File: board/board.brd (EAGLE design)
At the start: 94 x 44.5 mm, 71 parts, among them Q2 ULN2003AD

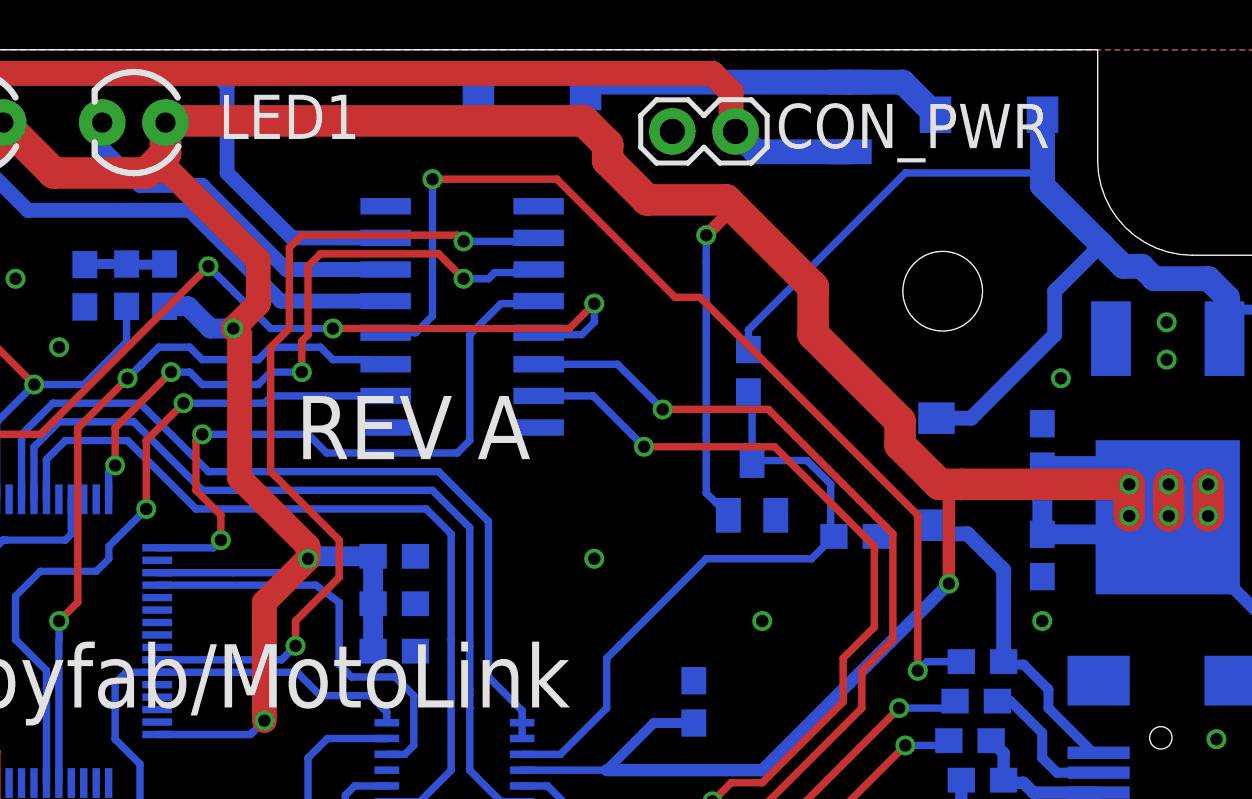
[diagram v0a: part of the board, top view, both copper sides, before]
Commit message: [Board] Adding output for external relay
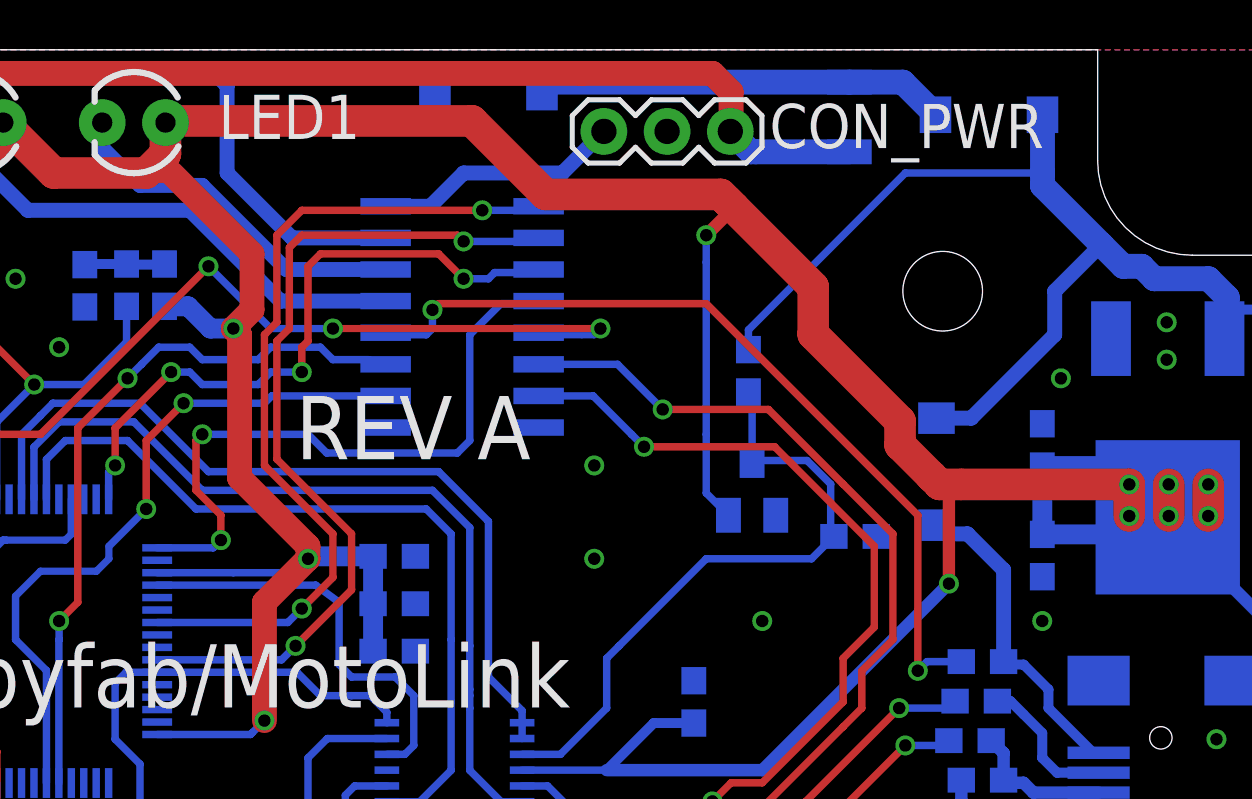
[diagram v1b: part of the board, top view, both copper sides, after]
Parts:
- CON_PWR: value M02PTH -> (none); device SparkFun-Connectors:1X02 -> SparkFun-Connectors:1X03
- IC_REG: value LD117ADT33TR -> NCV4274DT33RKG
- Y1: value (none) -> 8Mhz
- moved CON_PWR 2.75 mm to (65.9, 41.2)
- moved TVS1 1.75 mm to (61.2, 42.8)
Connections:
- new net RELAY_OUT: CON_PWR.1, Q2.16
- new net RELAY_TRIG: Q2.1, STM32.23
- net +12V: now also CON_PWR.3; no longer CON_PWR.2
- net GND: now also CON_PWR.2; no longer CON_PWR.1
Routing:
- net RELAY_TRIG: track 0.00 -> 33.9 mm, vias 0 -> 2
- net RELAY_OUT: track 0.00 -> 10.0 mm
- net N$7: track 40.9 -> 34.0 mm
- net N$9: track 14.8 -> 16.5 mm
- net USB_VBUS_CTRL: track 37.1 -> 36.3 mm

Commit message: [Board] Updated parts references
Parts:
- D1, D5, D6: value (none) -> B240A
- IC_REG: value NCV4274DT33RKG -> LM1117-3.3
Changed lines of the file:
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@@
 </autorouter>
 <elements>
-<element name="IC_REG" library="v-reg" package="DPACK" value="NCV4274DT33RKG" x="88.5425" y="28.045" smashed="yes" rot="MR180">
+<element name="IC_REG" library="v-reg" package="DPACK" value="LM1117-3.3" x="88.5425" y="28.045" smashed="yes" rot="MR180">
 <attribute name="NAME" x="84.3" y="22.33" size="1.778" layer="26" font="vector" ratio="16" rot="MR180"/>
 <attribute name="VALUE" x="93.6225" y="30.585" size="1.27" layer="28" rot="MR270"/>
@@
 <attribute name="VALUE" x="84.6455" y="25.146" size="0.4064" layer="28" font="vector" rot="MR270"/>
 </element>
-<element name="D1" library="SparkFun-DiscreteSemi" package="SMA-DIODE" value="" x="81.36" y="41.84" smashed="yes" rot="MR180">
+<element name="D1" library="SparkFun-DiscreteSemi" package="SMA-DIODE" value="B240A" x="81.36" y="41.84" smashed="yes" rot="MR180">
 <attribute name="NAME" x="81.824" y="39.939" size="1.778" layer="26" font="vector" ratio="16" rot="MR180"/>
 <attribute name="VALUE" x="81.614" y="40.189" size="0.4064" layer="28" rot="MR180"/>
@@
 <attribute name="VALUE" x="35.984" y="5.393" size="0.4064" layer="28" font="vector" rot="MR180"/>
 </element>
-<element name="D5" library="SparkFun-DiscreteSemi" package="SMA-DIODE" value="" x="79.25" y="27.5" smashed="yes" rot="MR90">
+<element name="D5" library="SparkFun-DiscreteSemi" package="SMA-DIODE" value="B240A" x="79.25" y="27.5" smashed="yes" rot="MR90">
 <attribute name="NAME" x="75.651" y="26.464" size="1.778" layer="26" font="vector" ratio="16" rot="MR90"/>
 <attribute name="VALUE" x="80.901" y="27.754" size="0.4064" layer="28" rot="MR90"/>
@@
 <attribute name="VALUE" x="10.516" y="23.107" size="0.4064" layer="28" font="vector" rot="MR0"/>
 </element>
-<element name="D6" library="SparkFun-DiscreteSemi" package="SMA-DIODE" value="" x="2.25" y="20.5" smashed="yes" rot="MR90">
+<element name="D6" library="SparkFun-DiscreteSemi" package="SMA-DIODE" value="B240A" x="2.25" y="20.5" smashed="yes" rot="MR90">
 <attribute name="NAME" x="3.901" y="18.964" size="1.778" layer="26" font="vector" ratio="16" rot="MR90"/>
 <attribute name="VALUE" x="3.901" y="20.754" size="0.4064" layer="28" rot="MR90"/>

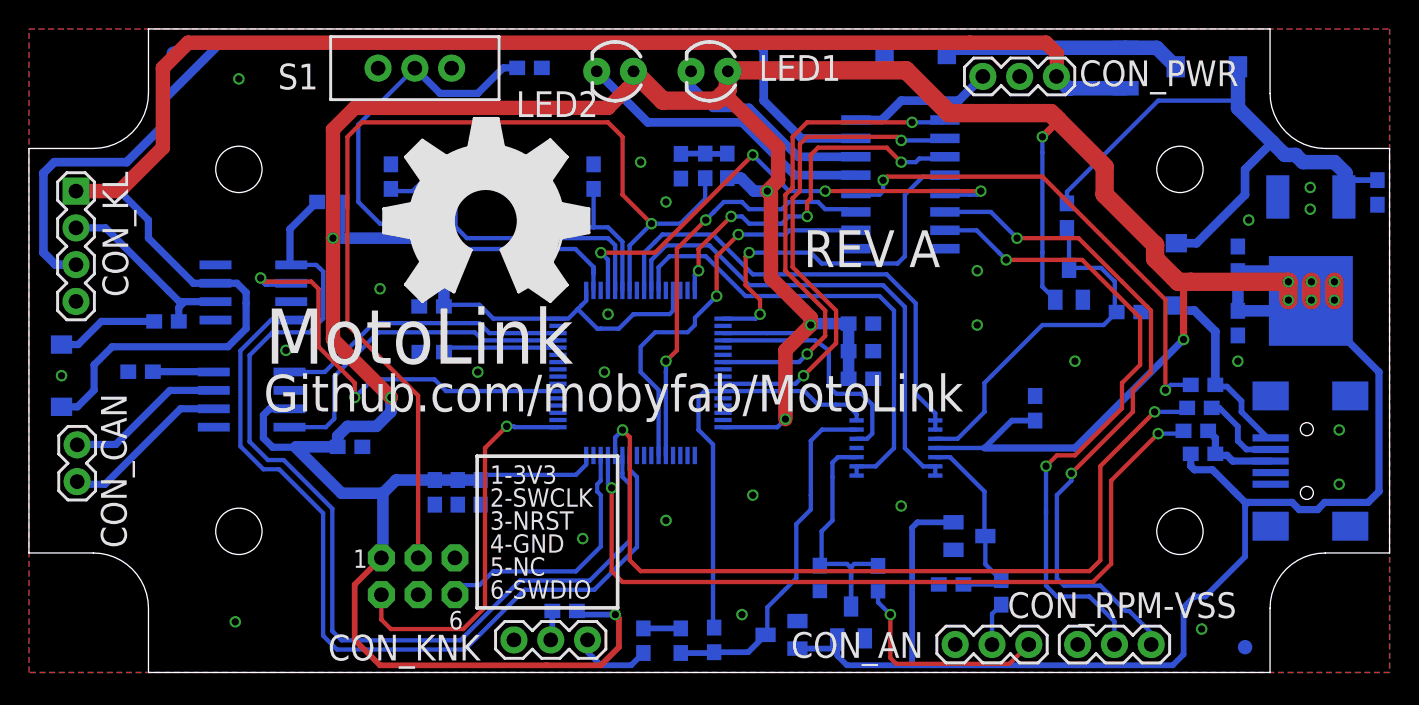
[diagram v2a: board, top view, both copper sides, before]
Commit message: [Board] Updated USB with esd/tvs protection, and vbus detection
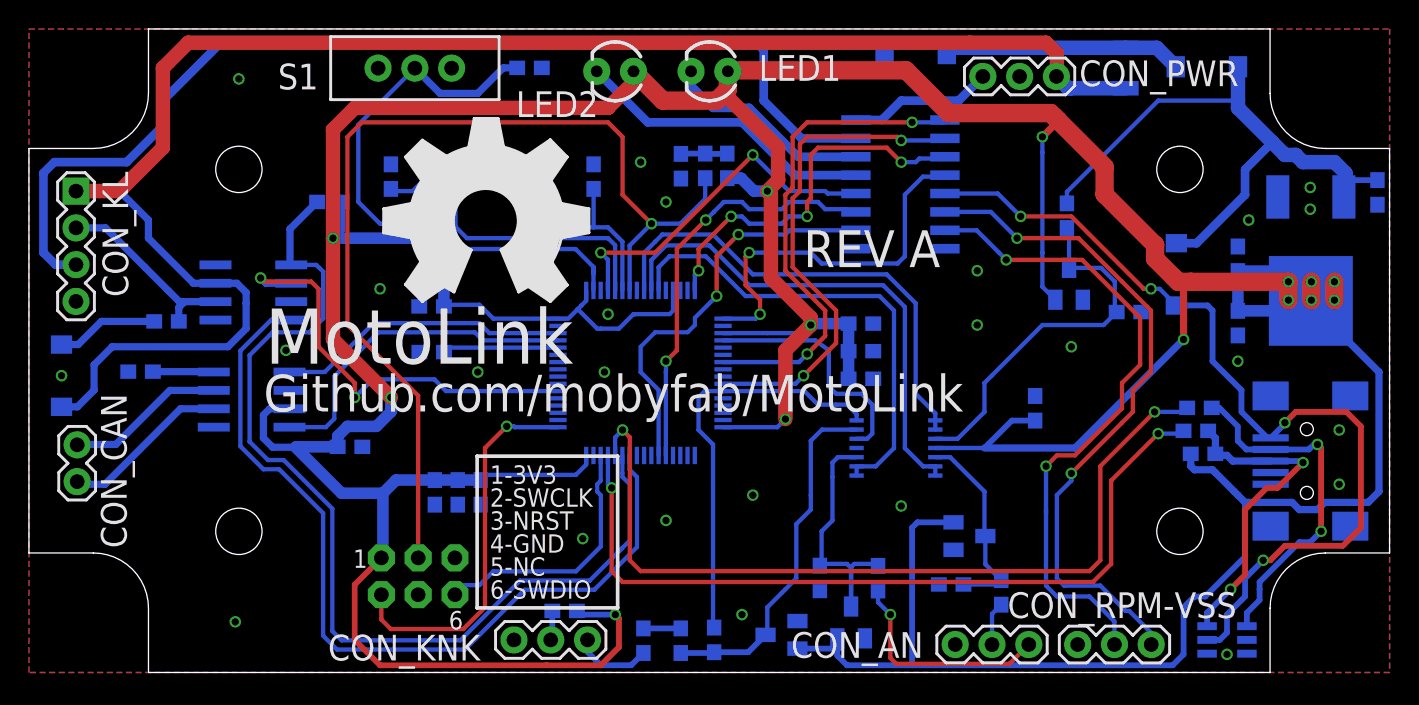
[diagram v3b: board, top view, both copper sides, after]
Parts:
- removed FID1, FID2: FIDUCIAL1X2, SparkFun-Aesthetics:FIDUCIAL-1X2
- removed R9: 1K, SparkFun-Resistors:0603-RES
- added TVS2: NUP4201MR6, misc:SOT23-6
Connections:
- removed net N$7: Q2.12, R9.1
- removed net USB_VBUS_CTRL: Q2.5, STM32.4
- new net USB_DETECT: Q2.12, STM32.4
- net GND: now also TVS2.2
- net N$17: now also TVS2.6
- net N$19: now also TVS2.1
- net OSC_IN: now also C7.2, STM32.5, Y1.2; no longer C5.2, STM32.6, Y1.1
- net OSC_OUT: now also C5.2, STM32.6, Y1.1; no longer C7.2, STM32.5, Y1.2
- net USB_VBUS: now also Q2.5, TVS2.5; no longer R9.2
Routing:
- net USB_VBUS: track 12.9 -> 62.1 mm, vias 0 -> 4
- net USB_VBUS_CTRL: track 36.3 -> 0.00 mm, vias 4 -> 0
- net N$7: track 34.0 -> 0.00 mm, vias 2 -> 0
- net USB_DETECT: track 0.00 -> 24.3 mm, vias 0 -> 2
- net N$19: track 5.84 -> 24.4 mm, vias 0 -> 2
- net N$17: track 5.82 -> 22.9 mm, vias 0 -> 2
- net OSC_OUT: track 23.0 -> 16.0 mm
- net OSC_IN: track 16.0 -> 23.0 mm

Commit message: [Board] Adding/Fixing USB detection and control
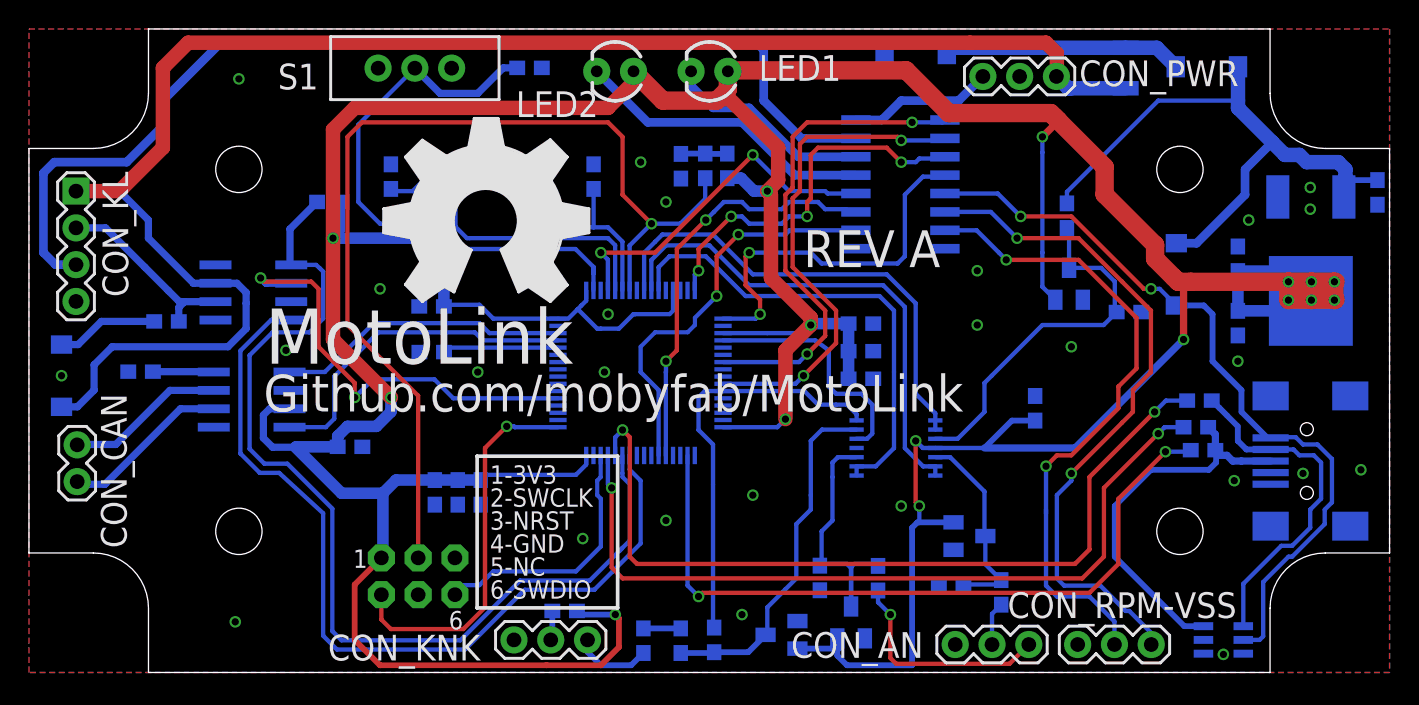
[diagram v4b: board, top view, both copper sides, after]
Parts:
- LED1: value (none) -> Green
- LED2: value (none) -> Blue
- R17: value 1K -> 1K5
- moved R16 0.50 mm to (80.8, 18.8)
- moved R15 0.25 mm to (80.6, 16.9)
- moved R17 0.25 mm to (81.1, 15.4)
- moved TVS2 0.25 mm to (82.5, 2.25), turned to 90 degrees
- renumbered JP1 to CON_USB
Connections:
- net LED1 renamed LED1_TRIG
- net LED2 renamed LED2_TRIG
- removed net N$19: CON_USB.D-, R16.1, TVS2.1
- new net N$7: CON_USB.D+, R15.1, R17.2, TVS2.3
- new net USB_CTRL: R17.1, STM32.34
- net +3V3: no longer R17.1
- net KL-CS: now also STM32.53; no longer STM32.54
- net N$17: now also CON_USB.D-, R16.1, TVS2.4; no longer CON_USB.D+, R15.1, R17.2, TVS2.6
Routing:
- net USB_CTRL: track 0.00 -> 50.9 mm, vias 0 -> 2
- net +3V3: track 401.1 -> 353.3 mm, vias 14 -> 16
- net N$7: track 0.00 -> 26.8 mm
- net N$19: track 24.4 -> 0.00 mm, vias 2 -> 0
- net USB_VBUS: track 62.1 -> 53.0 mm, vias 4 -> 2
- net USB_DM: track 58.9 -> 57.2 mm
- net USB_DP: track 55.8 -> 54.8 mm
- net N$17: track 22.9 -> 23.9 mm, vias 2 -> 0
- net N$21: track 45.5 -> 45.0 mm
